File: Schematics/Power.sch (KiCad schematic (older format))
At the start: 30 parts, among them J3 Barrel_Jack, U2 MCP16311MS, U3 LP2985-3.3, U4 LP2985-1.8

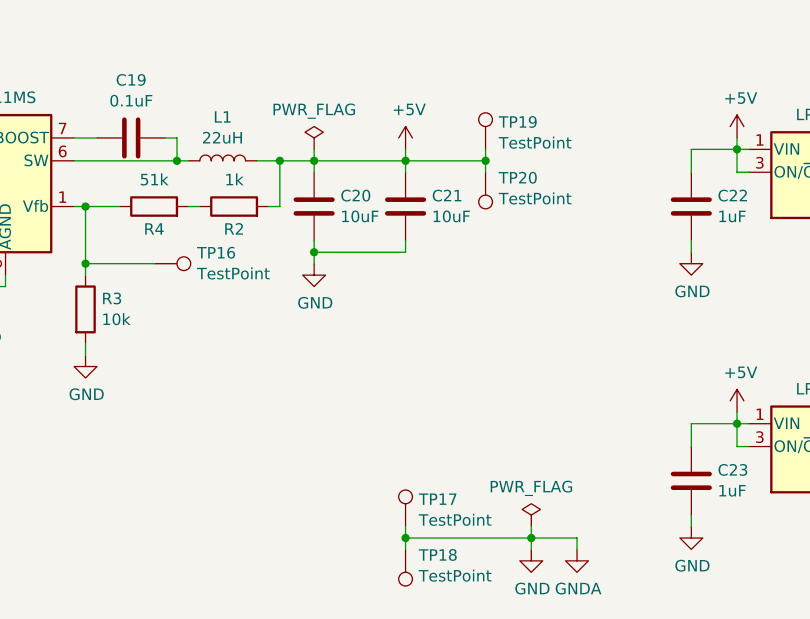
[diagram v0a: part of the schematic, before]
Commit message: Finished initial component placement
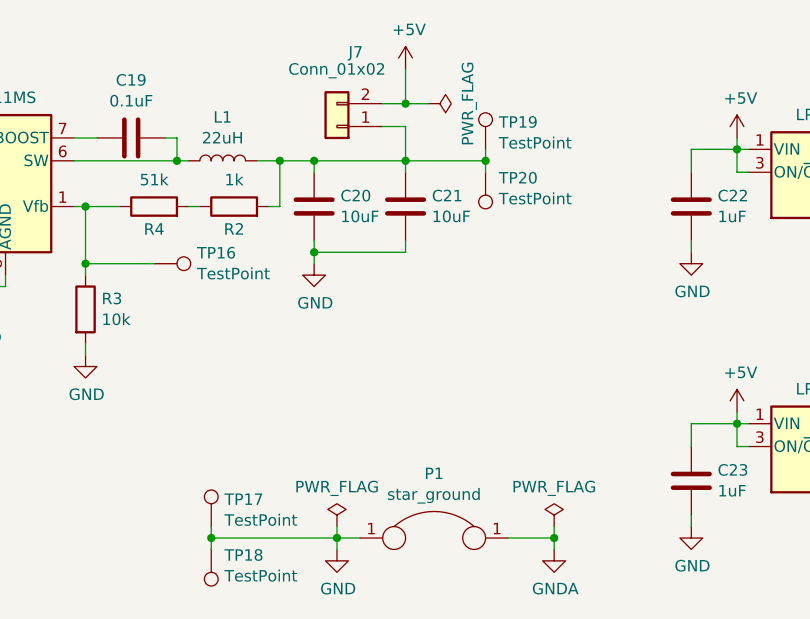
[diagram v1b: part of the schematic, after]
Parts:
- added J7: Conn_01x02, Connector_PinHeader_2.54mm:PinHeader_1x02_P2.54mm_Vertical, symbol Connector_Generic:Conn_01x02
- added P1: star_ground, Whitebox:star_ground, symbol Whitebox:star_ground
- L1: footprint Inductor_SMD:L_Vishay_IHLP-2020 -> Inductor_THT:L_Axial_L16.0mm_D6.3mm_P20.32mm_Horizontal_Fastron_VHBCC
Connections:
- net +5V: now also J7.2 (Pin_2); no longer C20.1, C21.1, L1.2, R2.2, TP19.1, TP20.1
- net GND: now also P1.1; no longer C24.2, C26.2, U3.2 (GND)
- new net: C20.1, C21.1, J7.1 (Pin_1), L1.2, R2.2, TP19.1, TP20.1
- new net GNDA: C24.2, C26.2, P1.1, U3.2 (GND)
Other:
- moved on the sheet: TP17, TP18
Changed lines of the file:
@@
 F 0 "L1" V 4540 2600 50  0000 C CNN
 F 1 "22uH" V 4449 2600 50  0000 C CNN
-F 2 "Inductor_SMD:L_Vishay_IHLP-2020" H 4350 2600 50  0001 C CNN
+F 2 "Inductor_THT:L_Axial_L16.0mm_D6.3mm_P20.32mm_Horizontal_Fastron_VHBCC" H 4350 2600 50  0001 C CNN
 F 3 "~" H 4350 2600 50  0001 C CNN
 	1    4350 2600
@@
 L power:PWR_FLAG #FLG01
 U 1 1 5EE75858
-P 4750 2550
-F 0 "#FLG01" H 4750 2625 50  0001 C CNN
-F 1 "PWR_FLAG" H 4750 2723 50  0000 C CNN
-F 2 "" H 4750 2550 50  0001 C CNN
-F 3 "~" H 4750 2550 50  0001 C CNN
-	1    4750 2550
-	1    0    0    -1
-$EndComp
-Wire Wire Line
-	4750 2550 4750 2600
-$Comp
-L power:+5V #PWR020
-U 1 1 5EE7637A
-P 5150 2550
-F 0 "#PWR020" H 5150 2400 50  0001 C CNN
-F 1 "+5V" H 5165 2723 50  0000 C CNN
-F 2 "" H 5150 2550 50  0001 C CNN
-F 3 "" H 5150 2550 50  0001 C CNN
-	1    5150 2550
-	1    0    0    -1
+P 5250 2350
+F 0 "#FLG01" H 5250 2425 50  0001 C CNN
+F 1 "PWR_FLAG" H 5250 2523 50  0000 C CNN
+F 2 "" H 5250 2350 50  0001 C CNN
+F 3 "~" H 5250 2350 50  0001 C CNN
+	1    5250 2350
+	0    1    1    0
 $EndComp
 $Comp
@@
 L power:GND #PWR021
 U 1 1 5EE8A626
-P 5700 4300
-F 0 "#PWR021" H 5700 4050 50  0001 C CNN
-F 1 "GND" H 5705 4127 50  0000 C CNN
-F 2 "" H 5700 4300 50  0001 C CNN
-F 3 "" H 5700 4300 50  0001 C CNN
-	1    5700 4300
-	1    0    0    -1
-$EndComp
-$Comp
-L power:GNDA #PWR022
-U 1 1 5EE8A8C4
-P 5900 4300
-F 0 "#PWR022" H 5900 4050 50  0001 C CNN
-F 1 "GNDA" H 5905 4127 50  0000 C CNN
-F 2 "" H 5900 4300 50  0001 C CNN
-F 3 "" H 5900 4300 50  0001 C CNN
-	1    5900 4300
-	1    0    0    -1
-$EndComp
-Wire Wire Line
-	5700 4300 5700 4250
-Wire Wire Line
-	5700 4250 5900 4250
-Wire Wire Line
-	5900 4250 5900 4300
+P 4850 4300
+F 0 "#PWR021" H 4850 4050 50  0001 C CNN
+F 1 "GND" H 4855 4127 50  0000 C CNN
+F 2 "" H 4850 4300 50  0001 C CNN
+F 3 "" H 4850 4300 50  0001 C CNN
+	1    4850 4300
+	1    0    0    -1
+$EndComp
+Wire Wire Line
+	4850 4300 4850 4250
+Wire Wire Line
+	5800 4250 5800 4300
 $Comp
 L Device:C C22
@@
 Wire Wire Line
 	4750 2600 5150 2600
-Wire Wire Line
-	5150 2550 5150 2600
 Connection ~ 5150 2600
 Wire Wire Line
@@
 L power:PWR_FLAG #FLG0102
 U 1 1 5F2C7F10
-P 5700 4200
-F 0 "#FLG0102" H 5700 4275 50  0001 C CNN
-F 1 "PWR_FLAG" H 5700 4373 50  0000 C CNN
-F 2 "" H 5700 4200 50  0001 C CNN
-F 3 "~" H 5700 4200 50  0001 C CNN
-	1    5700 4200
-	1    0    0    -1
-$EndComp
-Wire Wire Line
-	5700 4200 5700 4250
-Connection ~ 5700 4250
+P 4850 4200
+F 0 "#FLG0102" H 4850 4275 50  0001 C CNN
+F 1 "PWR_FLAG" H 4850 4373 50  0000 C CNN
+F 2 "" H 4850 4200 50  0001 C CNN
+F 3 "~" H 4850 4200 50  0001 C CNN
+	1    4850 4200
+	1    0    0    -1
+$EndComp
+Wire Wire Line
+	4850 4200 4850 4250
+Connection ~ 4850 4250
 $Comp
 L Device:R R2
@@
 L Connector:TestPoint TP17
 U 1 1 5F7EAD73
-P 5150 4200
-F 0 "TP17" H 5208 4318 50  0000 L CNN
-F 1 "TestPoint" H 5208 4227 50  0000 L CNN
-F 2 "TestPoint:TestPoint_Keystone_5010-5014_Multipurpose" H 5350 4200 50  0001 C CNN
-F 3 "~" H 5350 4200 50  0001 C CNN
-	1    5150 4200
+P 4300 4200
+F 0 "TP17" H 4358 4318 50  0000 L CNN
+F 1 "TestPoint" H 4358 4227 50  0000 L CNN
+F 2 "TestPoint:TestPoint_Keystone_5010-5014_Multipurpose" H 4500 4200 50  0001 C CNN
+F 3 "~" H 4500 4200 50  0001 C CNN
+	1    4300 4200
 	1    0    0    -1
 $EndComp
@@
 L Connector:TestPoint TP18
 U 1 1 5F7EB4F3
-P 5150 4300
-F 0 "TP18" H 5092 4326 50  0000 R CNN
-F 1 "TestPoint" H 5092 4417 50  0000 R CNN
-F 2 "TestPoint:TestPoint_Keystone_5010-5014_Multipurpose" H 5350 4300 50  0001 C CNN
-F 3 "~" H 5350 4300 50  0001 C CNN
-	1    5150 4300
+P 4300 4300
+F 0 "TP18" H 4242 4326 50  0000 R CNN
+F 1 "TestPoint" H 4242 4417 50  0000 R CNN
+F 2 "TestPoint:TestPoint_Keystone_5010-5014_Multipurpose" H 4500 4300 50  0001 C CNN
+F 3 "~" H 4500 4300 50  0001 C CNN
+	1    4300 4300
 	-1   0    0    1
 $EndComp
 Wire Wire Line
-	5700 4250 5150 4250
-Wire Wire Line
-	5150 4250 5150 4300
-Wire Wire Line
-	5150 4250 5150 4200
-Connection ~ 5150 4250
+	4850 4250 4300 4250
+Wire Wire Line
+	4300 4250 4300 4300
+Wire Wire Line
+	4300 4250 4300 4200
+Connection ~ 4300 4250
 Wire Wire Line
 	5150 2600 5500 2600
@@
 	5500 2650 5500 2600
 Connection ~ 5500 2600
+Wire Wire Line
+	5600 4250 5800 4250
+$Comp
+L power:GNDA #PWR022
+U 1 1 5EE8A8C4
+P 5800 4300
+F 0 "#PWR022" H 5800 4050 50  0001 C CNN
+F 1 "GNDA" H 5805 4127 50  0000 C CNN
+F 2 "" H 5800 4300 50  0001 C CNN
+F 3 "" H 5800 4300 50  0001 C CNN
+	1    5800 4300
+	1    0    0    -1
+$EndComp
+$Comp
+L power:PWR_FLAG #FLG0105
+U 1 1 5F00E720
+P 5800 4200
+F 0 "#FLG0105" H 5800 4275 50  0001 C CNN
+F 1 "PWR_FLAG" H 5800 4373 50  0000 C CNN
+F 2 "" H 5800 4200 50  0001 C CNN
+F 3 "~" H 5800 4200 50  0001 C CNN
+	1    5800 4200
+	1    0    0    -1
+$EndComp
+Wire Wire Line
+	5800 4200 5800 4250
+Connection ~ 5800 4250
+$Comp
+L Whitebox:star_ground P1
+U 1 1 5F021576
+P 5250 4250
+F 0 "P1" H 5275 4531 50  0000 C CNN
+F 1 "star_ground" H 5275 4440 50  0000 C CNN
+F 2 "Whitebox:star_ground" H 5550 4500 50  0001 C CNN
+F 3 "" H 5550 4500 50  0001 C CNN
+	1    5250 4250
+	1    0    0    -1
+$EndComp
+Wire Wire Line
+	4850 4250 4950 4250
+$Comp
+L Connector_Generic:Conn_01x02 J7
+U 1 1 5F197879
+P 4850 2450
+F 0 "J7" H 4768 2125 50  0000 C CNN
+F 1 "Conn_01x02" H 4850 2200 50  0000 C CNN
+F 2 "Connector_PinHeader_2.54mm:PinHeader_1x02_P2.54mm_Vertical" H 4850 2450 50  0001 C CNN
+F 3 "~" H 4850 2450 50  0001 C CNN
+	1    4850 2450
+	-1   0    0    1
+$EndComp
+$Comp
+L power:+5V #PWR020
+U 1 1 5F19AA1F
+P 5150 2200
+F 0 "#PWR020" H 5150 2050 50  0001 C CNN
+F 1 "+5V" H 5165 2373 50  0000 C CNN
+F 2 "" H 5150 2200 50  0001 C CNN
+F 3 "" H 5150 2200 50  0001 C CNN
+	1    5150 2200
+	1    0    0    -1
+$EndComp
+Wire Wire Line
+	5150 2450 5050 2450
+Wire Wire Line
+	5150 2450 5150 2600
+Wire Wire Line
+	5050 2350 5150 2350
+Wire Wire Line
+	5150 2350 5150 2200
+Connection ~ 5150 2350
+Wire Wire Line
+	5150 2350 5250 2350
 $EndSCHEMATC
